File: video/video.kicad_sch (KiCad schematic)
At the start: 37 parts, among them J1 Conn_02x20_Odd_Even, Q1 2N3904, Y1 10.7386Mhz

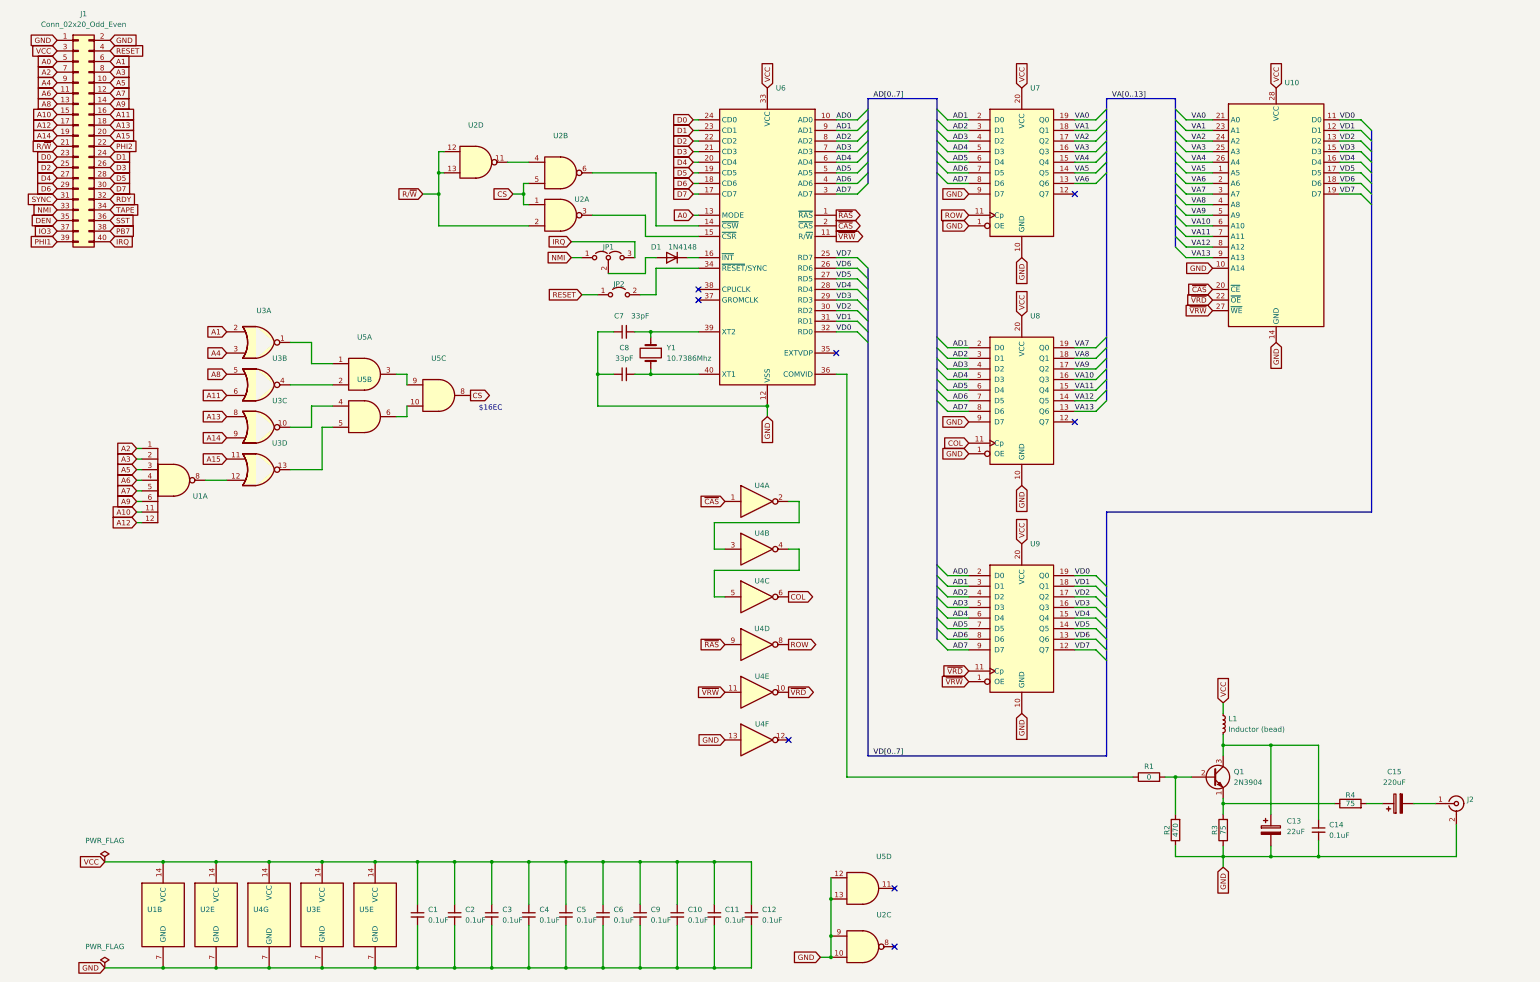
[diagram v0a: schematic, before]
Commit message: Initial pcb layout
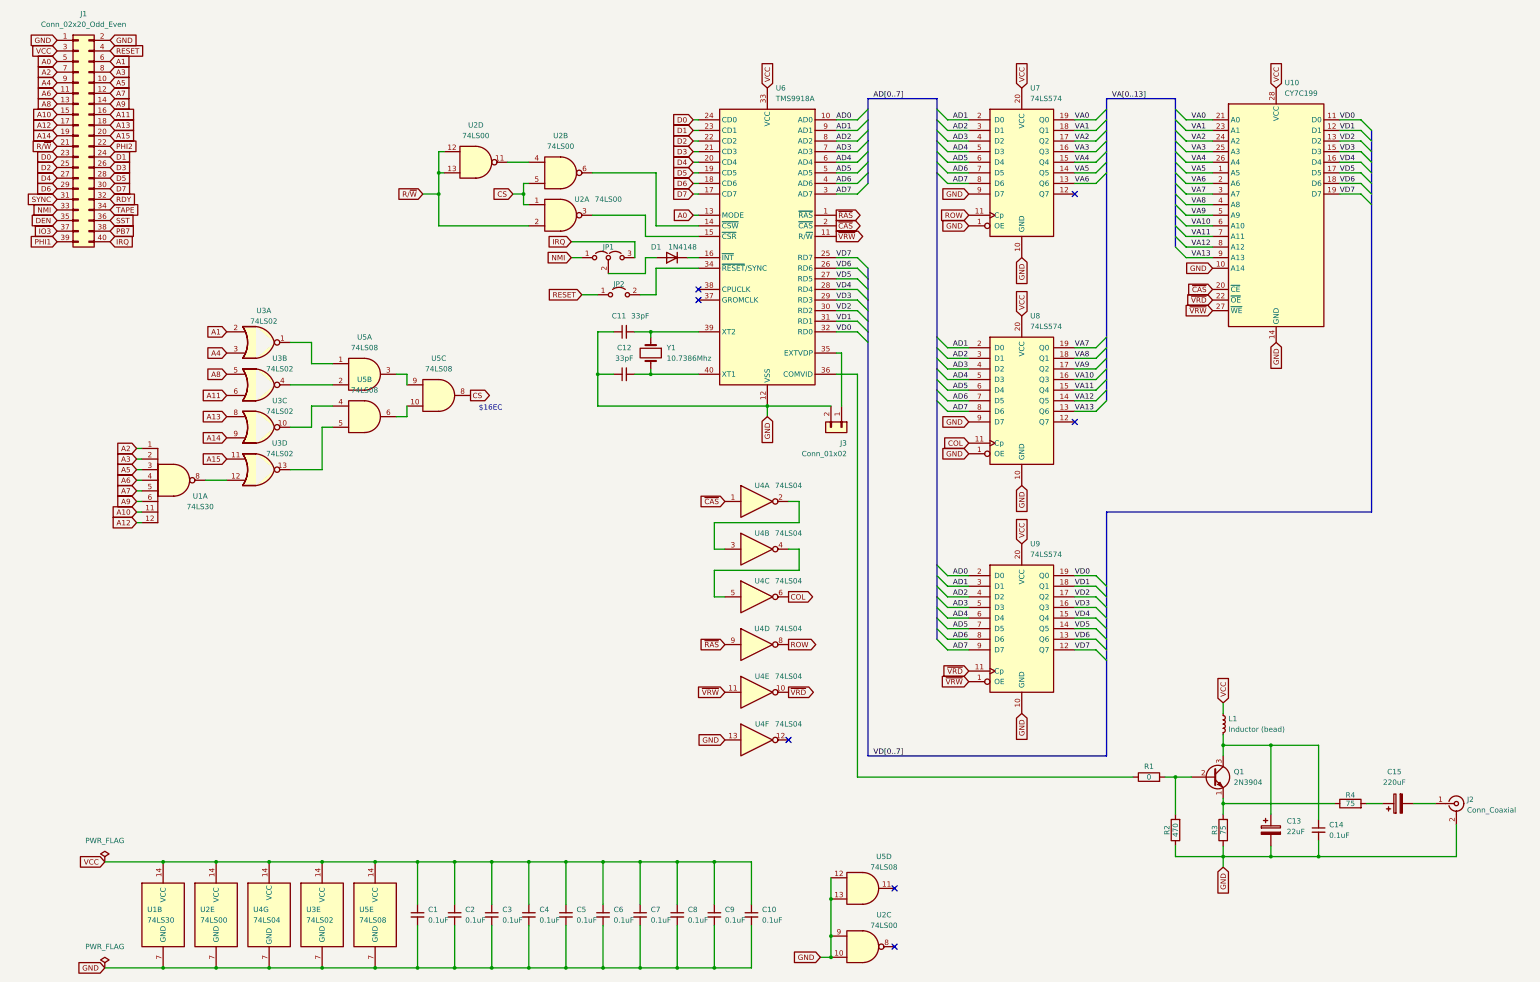
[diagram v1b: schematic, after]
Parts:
- added J3: Conn_01x02, Connector_PinHeader_2.54mm:PinHeader_1x02_P2.54mm_Vertical, symbol Connector_Generic:Conn_01x02
- C1, C14, C2, C3, C4, C5, C6: footprint (none) -> Capacitor_THT:C_Disc_D3.0mm_W1.6mm_P2.50mm
- C10: renamed from C12; footprint (none) -> Capacitor_THT:C_Disc_D3.0mm_W1.6mm_P2.50mm
- C11: renamed from C7; footprint (none) -> Capacitor_THT:C_Disc_D4.7mm_W2.5mm_P5.00mm
- C12: renamed from C8; footprint (none) -> Capacitor_THT:C_Disc_D4.7mm_W2.5mm_P5.00mm
- C13, C15: footprint (none) -> Capacitor_THT:CP_Radial_D5.0mm_P2.50mm
- C7: renamed from C9; footprint (none) -> Capacitor_THT:C_Disc_D3.0mm_W1.6mm_P2.50mm
- C8: renamed from C10; footprint (none) -> Capacitor_THT:C_Disc_D3.0mm_W1.6mm_P2.50mm
- C9: renamed from C11; footprint (none) -> Capacitor_THT:C_Disc_D3.0mm_W1.6mm_P2.50mm
- J2: value (none) -> Conn_Coaxial; footprint (none) -> Video:RCA right angle phono
- JP1: value (none) -> Jumper_3_Open; footprint (none) -> Connector_PinHeader_2.54mm:PinHeader_1x03_P2.54mm_Vertical
- JP2: footprint (none) -> Connector_PinHeader_2.54mm:PinHeader_1x02_P2.54mm_Vertical
- L1: footprint (none) -> Inductor_THT:L_Axial_L7.0mm_D3.3mm_P10.16mm_Horizontal_Fastron_MICC
- R1, R2, R3, R4: footprint (none) -> Resistor_THT:R_Axial_DIN0207_L6.3mm_D2.5mm_P7.62mm_Horizontal
- U1: value (none) -> 74LS30; footprint (none) -> Package_DIP:DIP-14_W7.62mm
- U10: value (none) -> CY7C199; footprint (none) -> Package_DIP:DIP-28_W7.62mm
- U2: value (none) -> 74LS00; footprint (none) -> Package_DIP:DIP-14_W7.62mm
- U3: value (none) -> 74LS02; footprint (none) -> Package_DIP:DIP-14_W7.62mm
- U4: value (none) -> 74LS04; footprint (none) -> Package_DIP:DIP-14_W7.62mm
- U5: value (none) -> 74LS08; footprint (none) -> Package_DIP:DIP-14_W7.62mm
- U6: value (none) -> TMS9918A; footprint (none) -> Package_DIP:DIP-40_W15.24mm
- U7, U8, U9: value (none) -> 74LS574; footprint (none) -> Package_DIP:DIP-20_W7.62mm
- Y1: footprint (none) -> Crystal:Crystal_HC49-U_Vertical
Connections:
- net GND: now also J3.2 (Pin_2)
- net at U6.35 (EXTVDP): now also J3.1 (Pin_1)
- no-connect marks 8 -> 7
